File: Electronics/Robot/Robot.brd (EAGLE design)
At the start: 76.2 x 59.4 mm, 23 parts, among them Q1 2N7000, Q2 2N7000, U1 GY-521MPU6050, U2 SN74LS241N

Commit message: Fixed Gears and made PCB
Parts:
- removed JP1: B3B-PH-K-S, con-JST PH:B3B-PH-K-S
- added X2: JST-XH-03-PIN-ROUND-PAD, JST XH Connectors v1-0:JST-XH-03-PACKAGE-ROUND-PAD
- moved U$1 162.0 mm to (31.8, 40.6), turned to 270 degrees
- moved T1 139.1 mm to (12.7, 30.5), turned to 180 degrees
- moved R4 138.3 mm to (17.8, 30.5), turned to 90 degrees
- moved SG1 137.9 mm to (10.2, 43.2), turned to 270 degrees
- moved C1 95.6 mm to (27.9, 16.5), turned to 270 degrees
- moved X1 90.4 mm to (29.2, 3.81), turned to 180 degrees
- moved R3 89.2 mm to (48.3, 7.62), turned to 180 degrees
- moved U2 84.5 mm to (54.6, 20.3), turned to 90 degrees
- moved U$3 81.8 mm to (38.1, 3.81)
- moved U$2 80.8 mm to (48.3, 3.81)
- moved R13 11.7 mm to (53.3, 54.6)
- moved R14 11.7 mm to (53.3, 47.0)
- moved R15 11.7 mm to (53.3, 57.1)
- moved R16 11.7 mm to (53.3, 49.5)
- moved Q1 11.7 mm to (62.2, 55.9)
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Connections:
- net ENABLE_AX12: now also U$1.20
- net GND: now also X2.3; no longer JP1.3
- net RX_AX12: now also U$1.17
- net SSC-32-RX: now also X2.2; no longer JP1.2
- net SSC-32-TX: now also X2.1; no longer JP1.1
- net TX_AX12: now also U$1.16
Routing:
- added copper zone on layer 16, net GND

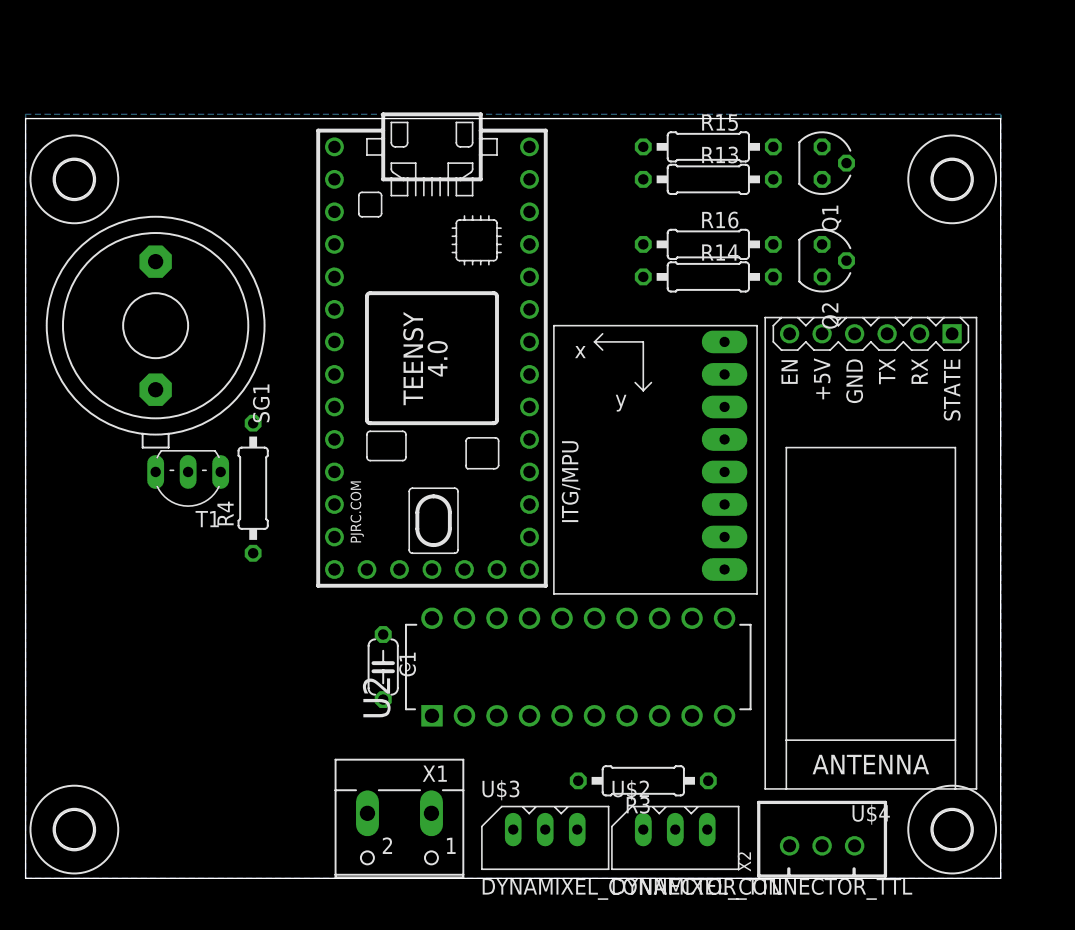
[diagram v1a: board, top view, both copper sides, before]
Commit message: 5V added & better layout
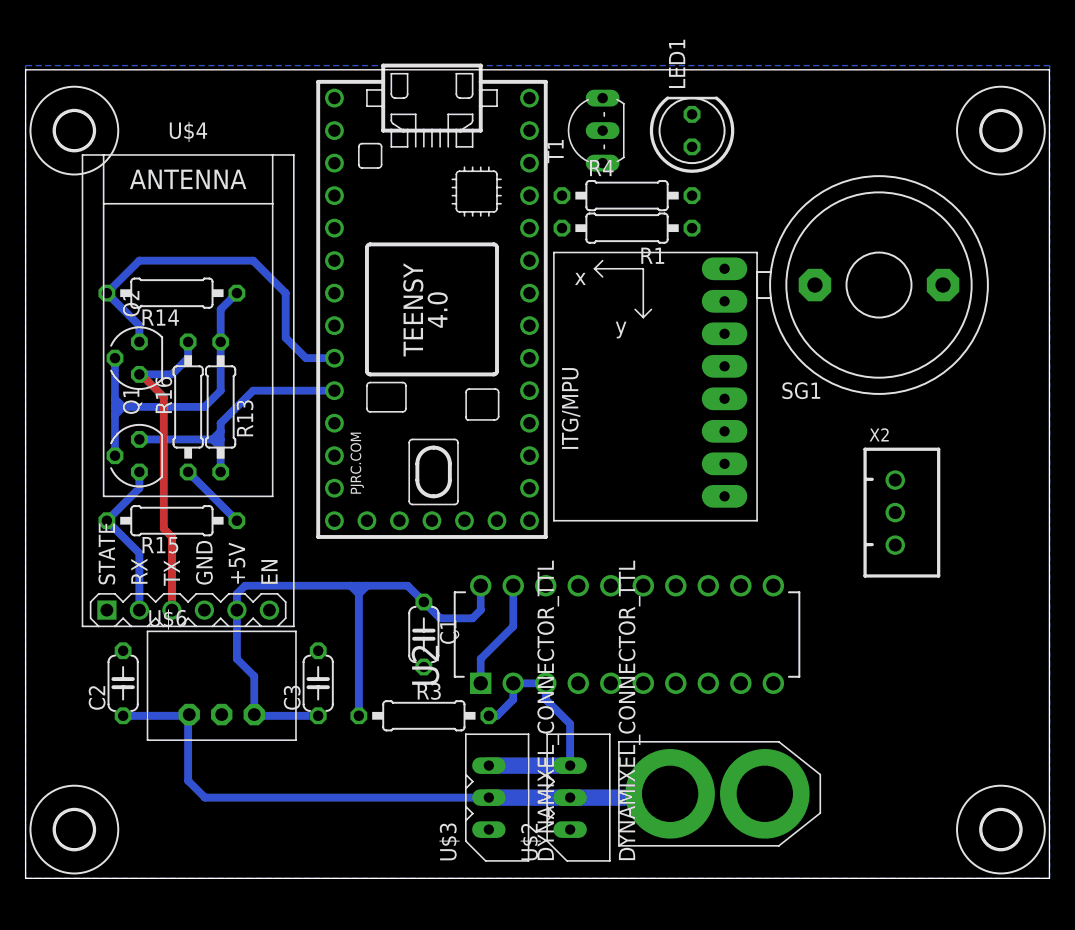
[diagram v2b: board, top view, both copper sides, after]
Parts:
- removed X1: (no value), con-wago-500:W237-102
- added C2, C3: 10uF, rcl:C050-024X044
- added LED1: (no value), led:LED5MM
- added R1: 220, rcl:0207/10
- added U$5: XT60, XT60:XT60
- added U$6: R-78E5.0-0.5, Power:R-78E5.0-0.5
- moved Q1 58.0 mm to (8.89, 33.0), turned to 90 degrees
- moved SG1 56.6 mm to (66.7, 46.4), turned to 180 degrees
- moved U$4 54.8 mm to (12.7, 38.1), turned to 0 degrees
- moved Q2 53.9 mm to (8.89, 40.6), turned to 90 degrees
- moved R15 51.1 mm to (11.4, 27.9), turned to 180 degrees
- moved R16 42.6 mm to (12.7, 36.8), turned to 90 degrees
- moved R13 42.0 mm to (15.2, 36.8), turned to 270 degrees
- moved R14 41.9 mm to (11.4, 45.7), turned to 180 degrees
- moved T1 41.8 mm to (43.8, 58.4), turned to 90 degrees
- moved R4 37.1 mm to (47.0, 53.3), turned to 0 degrees
- moved X2 26.7 mm to (67.9, 28.6), turned to 270 degrees
- moved R3 17.9 mm to (31.1, 12.7), turned to 0 degrees
- moved U$2 5.71 mm to (42.5, 3.81), turned to 90 degrees
- moved U1 5.71 mm to (45.7, 38.7)
- moved H4 5.39 mm to (76.2, 58.4)
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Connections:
- new net N$5: LED1.A, R1.1
- net +12V: now also C2.1, U$5.+, U$6.VIN; no longer X1.1
- net +5V: now also C3.1, R1.2, U$6.VOUT
- net GND: now also C2.2, C3.2, LED1.K, U$5.-, U$6.GND; no longer X1.2
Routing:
- net +5V: track 0.00 -> 49.5 mm
- net +12V: track 0.00 -> 48.7 mm
- net BL_TX: track 0.00 -> 28.9 mm
- net N$1: track 0.00 -> 26.3 mm
- net N$1001: track 0.00 -> 25.1 mm
- net BL_RX: track 0.00 -> 21.9 mm
- net DATA: track 0.00 -> 19.8 mm
- net N$100: track 0.00 -> 12.9 mm
- net ENABLE_AX12: track 0.00 -> 8.67 mm
- net N$3: track 0.00 -> 5.39 mm
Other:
- board size 76.2 x 59.4 mm -> 80 x 63.2 mm
